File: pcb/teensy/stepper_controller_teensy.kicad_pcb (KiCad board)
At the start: 2 copper layers, 69.8 x 40.6 mm, 15 parts, among them P1 HEADER_02X08_SMD, SW1 SPST_SLIDE_AS, U1 TLE7230R

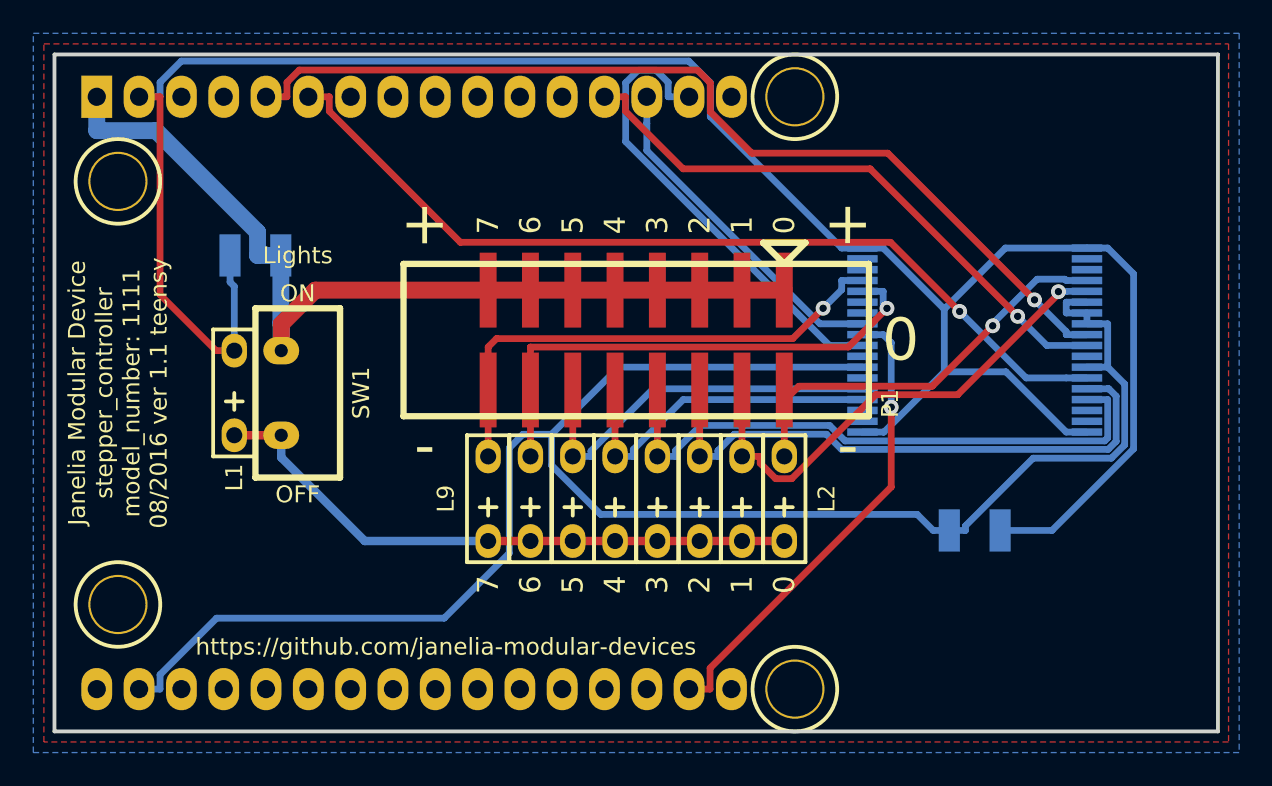
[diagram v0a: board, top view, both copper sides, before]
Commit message: Added L6470.
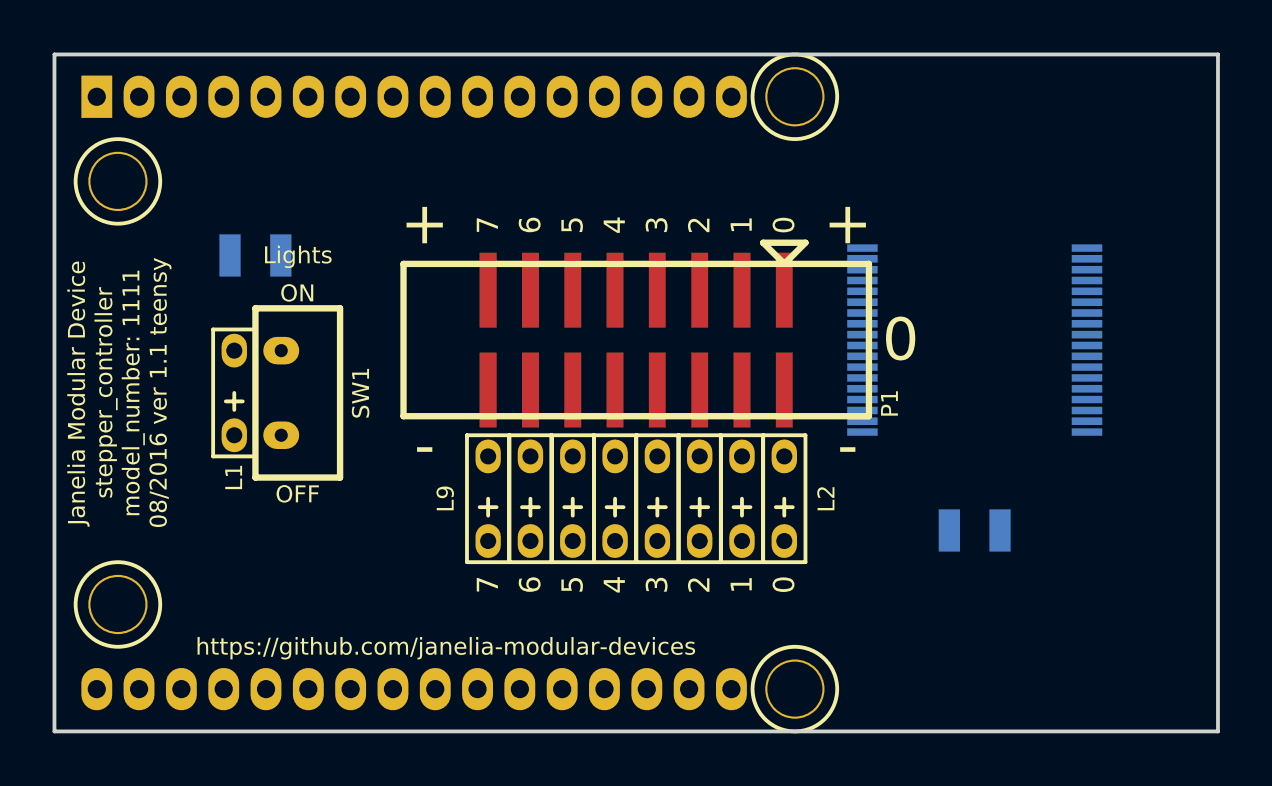
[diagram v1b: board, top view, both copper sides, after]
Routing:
- net GND: track 136.2 -> 0.00 mm
- net VEE: track 109.8 -> 0.00 mm
- net /RESET: track 58.2 -> 0.00 mm, vias 1 -> 0
- net VDD: track 55.4 -> 0.00 mm
- net /PWM: track 54.2 -> 0.00 mm, vias 1 -> 0
- net /LED_PWR: track 36.4 -> 0.00 mm
- net /OUT3: track 36.0 -> 0.00 mm
- net /CS: track 35.7 -> 0.00 mm, vias 1 -> 0
- net /OUT2: track 35.0 -> 0.00 mm
- net /OUT6: track 31.3 -> 0.00 mm, vias 1 -> 0
- net /OUT7: track 31.0 -> 0.00 mm, vias 1 -> 0
- net /OUT1: track 30.2 -> 0.00 mm, vias 1 -> 0
- net /SCK: track 28.5 -> 0.00 mm, vias 1 -> 0
- net /MISO: track 28.1 -> 0.00 mm
- net /OUT0: track 25.3 -> 0.00 mm, vias 1 -> 0
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- removed copper zone on B.Cu, net GND
- removed copper zone on F.Cu, net VDD

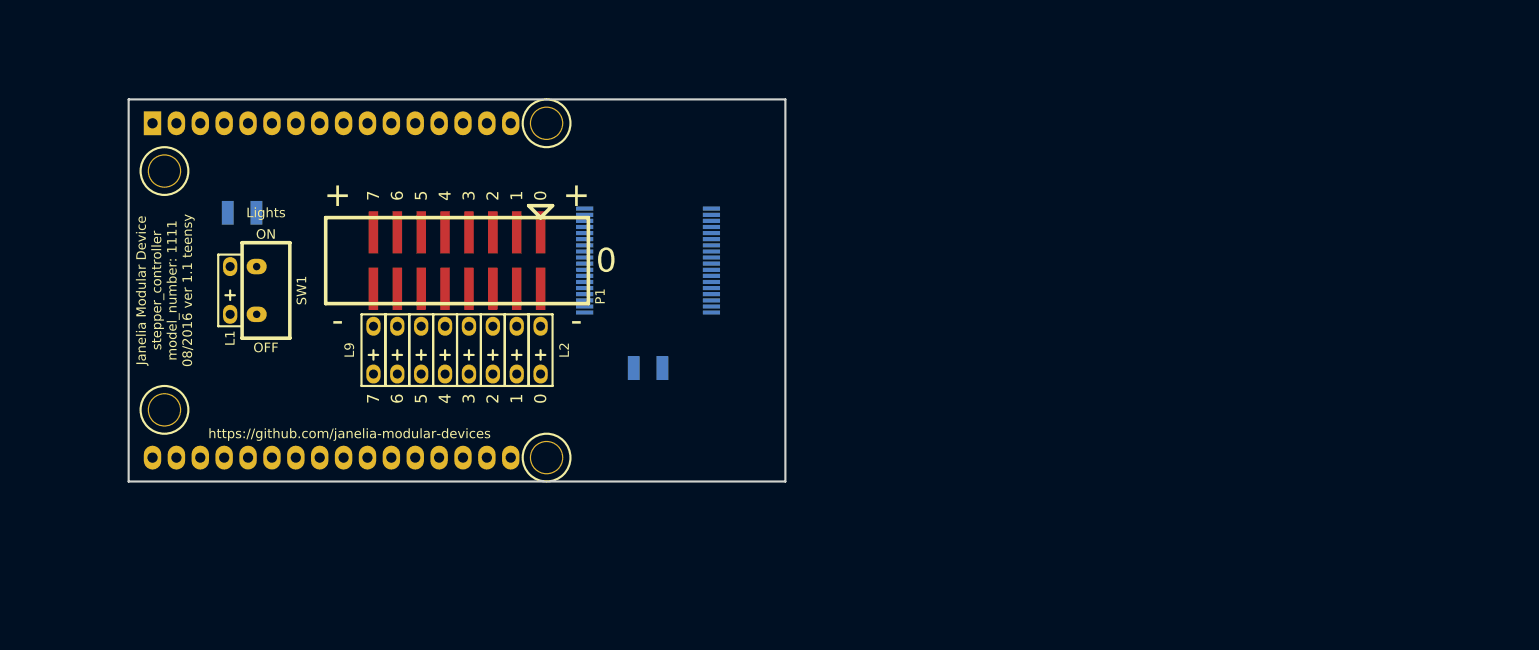
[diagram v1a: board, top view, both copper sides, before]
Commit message: Adjusted footprints.
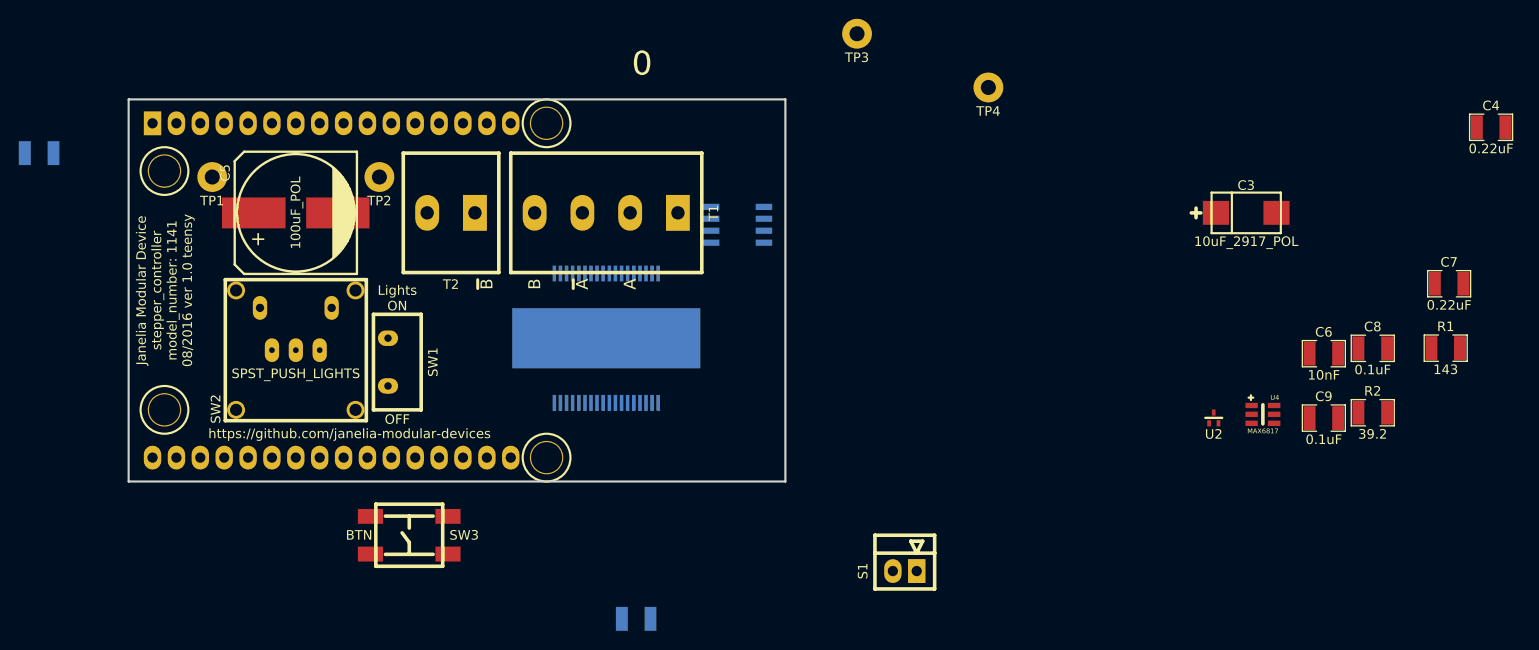
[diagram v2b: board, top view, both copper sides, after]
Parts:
- removed L1, L2, L3, L4, L5, L6, L7, L8, L9: LED_24V, stepper_controller_teensy:LED_555-3XXX
- removed P1: HEADER_02X08_SMD, stepper_controller_teensy:HEADER_02x08_SMD
- added C3: 10uF_2917_POL, stepper_controller_teensy:SM2917_POL, F.Cu at (192.5, 91.4)
- added C4: 0.22uF, stepper_controller_teensy:SM1210, F.Cu at (218.6, 82.3)
- added C5: 100uF_POL, stepper_controller_teensy:C_ELEC_12.5, F.Cu at (91.4, 91.4)
- added C6: 10nF, stepper_controller_teensy:SM1210, F.Cu at (200.8, 106.4)
- added C7: 0.22uF, stepper_controller_teensy:SM1210, F.Cu at (214.1, 99.0)
- added C8: 0.1uF, stepper_controller_teensy:SM1210, F.Cu at (206.0, 105.9)
- added C9: 0.1uF, stepper_controller_teensy:SM1210, F.Cu at (200.8, 113.3)
- added R1: 143, stepper_controller_teensy:SM1210, F.Cu at (213.7, 105.8)
- added R2: 39.2, stepper_controller_teensy:SM1210, F.Cu at (206.0, 112.7)
- added S1: HEADER_01X02_SHR, stepper_controller_teensy:Header_Shrouded_2_Pin, F.Cu at (156.2, 129.5)
- added SW2: SPST_PUSH_LIGHTS, stepper_controller_teensy:KP_SWITCH, F.Cu at (91.4, 106.0)
- added SW3: KT_SWITCH, stepper_controller_teensy:KT_SWITCH, F.Cu at (103.5, 125.7)
- added T1: TERM_BLK_ANG_4_PIN_0.2_PITCH, footprints:TERM_BLK_ANG_4_PIN_0.2_PITCH, F.Cu at (124.5, 91.4)
- added T2: TERM_BLK_ANG_2_PIN_0.2_PITCH, footprints:TERM_BLK_ANG_2_PIN_0.2_PITCH, F.Cu at (108.0, 91.4)
- added TP1: TESTPOINT_RED, footprints:TESTPOINT_THRU, F.Cu at (82.5, 87.6)
- added TP2: TESTPOINT_BLK, footprints:TESTPOINT_THRU, F.Cu at (100.3, 87.6)
- added TP3: TESTPOINT_WHT, footprints:TESTPOINT_THRU, F.Cu at (151.1, 72.4)
- added TP4: TESTPOINT_BLK, footprints:TESTPOINT_THRU, F.Cu at (165.1, 78.1)
- added U2: BAV99T, stepper_controller_teensy:SOT-523, F.Cu at (189.1, 113.2)
- added U3: CUR_SEN_+/-5A, footprints:SOIC_8_LC, B.Cu at (138.4, 92.7)
- added U4: MAX6817, stepper_controller_teensy:MAX6817, F.Cu at (194.3, 112.9)
- C1: value 10uF -> 0.1uF
- U1: value TLE7230R -> L6470; footprint stepper_controller_teensy:PG-DSO-36 -> stepper_controller_teensy:POWERSO-36
- moved C2 26.7 mm to (127.6, 134.6)
- moved C1 22.5 mm to (64.1, 85.1)
- moved SW1 15.9 mm to (102.2, 107.3)
- moved U1 9.38 mm to (124.5, 104.8), turned to 0 degrees
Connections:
- C1 pad 1: VDD -> +3V3
- C2 pad 1: VEE -> +3V3
- MDT1 pad 14: (no net) -> /VIOUT
- MDT1 pad 16: (no net) -> /LED_RED
- MDT1 pad 17: (no net) -> /LED_GREEN
- MDT1 pad 3: /PWM -> /FLAG
- MDT1 pad 3V3: (no net) -> +3V3
- MDT1 pad 4: (no net) -> /BUSY
- MDT1 pad 5: (no net) -> /ACTION
- MDT1 pad VEE: VEE -> (no net)
- SW1 pad 1: VDD -> +3V3
- U1 pad 10: /CS -> (no net)
- U1 pad 12: VEE -> GND
- U1 pad 13: /PWM -> /CP
- U1 pad 14: /OUT2 -> /VBOOT
- U1 pad 15: /OUT3 -> VDD
- U1 pad 16: (no net) -> VDD
- U1 pad 17: (no net) -> /OUT1B
- U1 pad 18: GND -> /OUT1B
- U1 pad 2: (no net) -> /OUT1A_0
- U1 pad 20: (no net) -> /OUT2B
- U1 pad 21: (no net) -> /OUT2B
- U1 pad 22: /OUT4 -> VDD
- U1 pad 23: /OUT5 -> VDD
- U1 pad 24: (no net) -> +3V3
- U1 pad 25: VEE -> /MISO
- U1 pad 26: (no net) -> /SCK
- U1 pad 27: /MISO -> /MOSI
- U1 pad 28: /SCK -> GND
- U1 pad 29: /MOSI -> /BUSY
- U1 pad 3: (no net) -> /OUT1A_0
- U1 pad 30: (no net) -> /CS
- U1 pad 31: (no net) -> /FLAG
- U1 pad 32: /OUT6 -> GND
- U1 pad 33: /OUT7 -> VDD
- U1 pad 34: (no net) -> VDD
- U1 pad 35: (no net) -> /OUT2A
- U1 pad 36: GND -> /OUT2A
- U1 pad 4: /OUT0 -> VDD
- U1 pad 5: /OUT1 -> VDD
- U1 pad 6: VEE -> /RESET
- U1 pad 7: VEE -> /SW
- U1 pad 8: VEE -> GND
- U1 pad 9: /RESET -> +3V3
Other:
- board text added: "A"
- board text added: "B"
- board text added: "Janelia Modular Device stepper_controller model_number: 1141 08/2016 ver 1.0 teensy"
- board text added: "~A"
- board text added: "~B"
- board text removed: "+"
- board text removed: "-"
- board text removed: "1"
- board text removed: "2"
- board text removed: "3"
- board text removed: "4"
- board text removed: "5"
- board text removed: "6"
- board text removed: "7"
- board text removed: "Janelia Modular Device stepper_controller model_number: 1111 08/2016 ver 1.1 teensy"

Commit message: Finished teensy pcb v1.0.
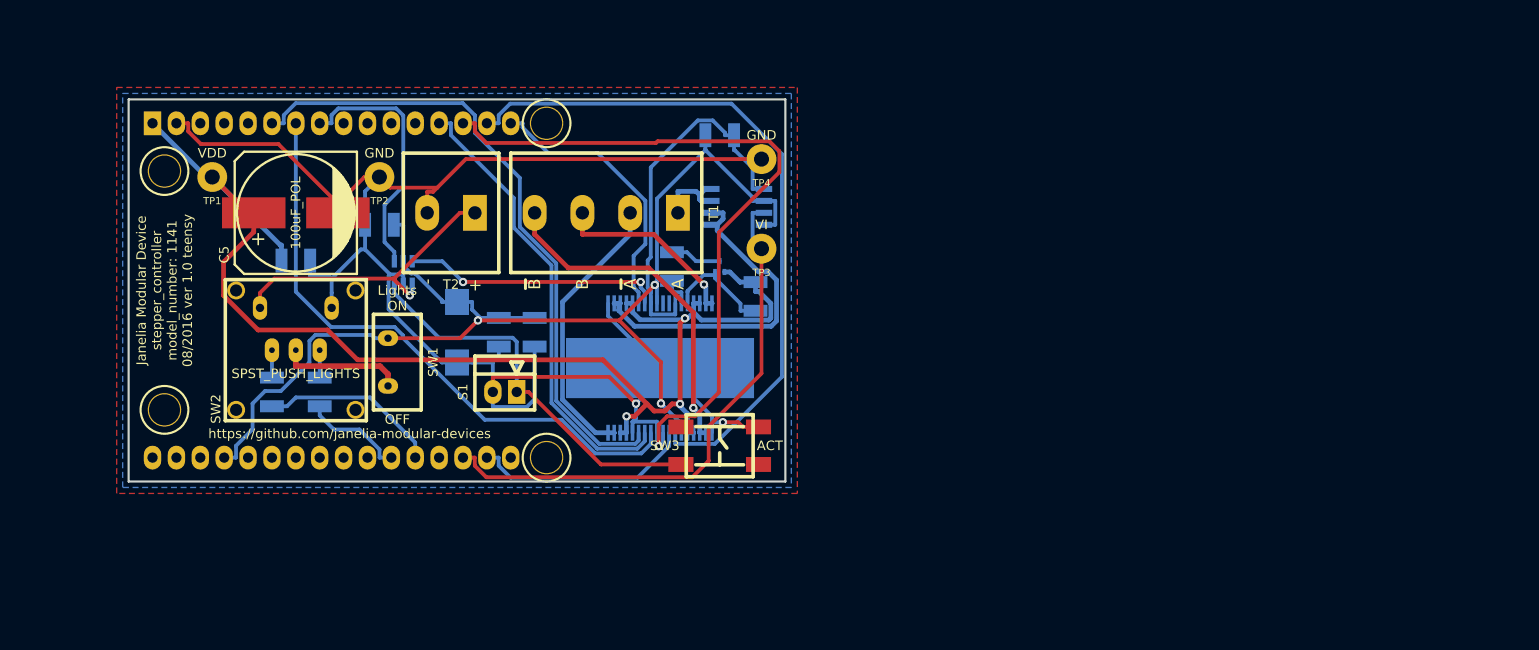
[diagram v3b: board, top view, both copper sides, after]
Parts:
- C3, C4, C6, C7, C8, C9, R1, R2, U2, U4: moved to B.Cu
- T1: footprint footprints:TERM_BLK_ANG_4_PIN_0.2_PITCH -> stepper_controller_teensy:TERM_BLK_ANG_4_PIN_0.2_PITCH
- T2: footprint footprints:TERM_BLK_ANG_2_PIN_0.2_PITCH -> stepper_controller_teensy:TERM_BLK_ANG_2_PIN_0.2_PITCH
- TP1, TP2, TP3, TP4: footprint footprints:TESTPOINT_THRU -> stepper_controller_teensy:TESTPOINT_THRU
- U3: footprint footprints:SOIC_8_LC -> stepper_controller_teensy:SOIC_8_LC
- moved C4 127.9 mm to (91.4, 96.5), turned to 180 degrees
- moved R1 124.9 mm to (88.9, 110.5), turned to 270 degrees
- moved R2 112.0 mm to (94.0, 110.5), turned to 270 degrees
- moved C9 102.5 mm to (100.3, 92.7), turned to 180 degrees
- moved U4 92.7 mm to (102.9, 97.8), turned to 90 degrees
- moved C3 84.9 mm to (108.6, 104.1), turned to 270 degrees
- moved C7 73.8 mm to (140.3, 100.3), turned to 270 degrees
- moved C8 73.1 mm to (136.5, 83.2)
- moved C6 70.0 mm to (131.4, 97.2), turned to 90 degrees
- moved C1 56.0 mm to (116.8, 104.1), turned to 270 degrees
- moved U2 55.0 mm to (136.5, 97.2), turned to 180 degrees
- moved S1 46.6 mm to (113.7, 110.5)
- moved SW3 34.4 mm to (136.5, 116.2), turned to 180 degrees
- moved C2 33.8 mm to (113.0, 104.1), turned to 270 degrees
- moved TP4 25.3 mm to (141.0, 85.7)
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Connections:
- MDT1 pad 15: (no net) -> Net-(MDT1-Pad15)
- MDT1 pad 18: (no net) -> Net-(MDT1-Pad18)
- MDT1 pad 19: (no net) -> Net-(MDT1-Pad19)
- MDT1 pad 2: /RESET -> Net-(MDT1-Pad2)
- MDT1 pad 20: (no net) -> Net-(MDT1-Pad20)
- MDT1 pad 21: (no net) -> Net-(MDT1-Pad21)
- MDT1 pad 22: (no net) -> Net-(MDT1-Pad22)
- MDT1 pad 23: (no net) -> Net-(MDT1-Pad23)
- MDT1 pad 24: (no net) -> Net-(MDT1-Pad24)
- MDT1 pad 25: (no net) -> Net-(MDT1-Pad25)
- MDT1 pad 28: (no net) -> /RESET
- MDT1 pad 29: (no net) -> Net-(MDT1-Pad29)
- MDT1 pad 30: (no net) -> Net-(MDT1-Pad30)
- MDT1 pad 6: (no net) -> Net-(MDT1-Pad6)
- MDT1 pad 9: (no net) -> Net-(MDT1-Pad9)
- MDT1 pad AGND: (no net) -> Net-(MDT1-PadAGND)
- MDT1 pad AREF: (no net) -> Net-(MDT1-PadAREF)
- MDT1 pad DAC: (no net) -> Net-(MDT1-PadDAC)
- MDT1 pad VEE: (no net) -> Net-(MDT1-PadVEE)
- U1 pad 10: (no net) -> Net-(U1-Pad10)
- U1 pad 11: (no net) -> Net-(U1-Pad11)
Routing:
- net GND: track 0.00 -> 228.1 mm, vias 0 -> 2
- net VDD: track 0.00 -> 136.8 mm, vias 0 -> 3
- net +3V3: track 0.00 -> 128.6 mm, vias 0 -> 3
- net /MOSI: track 0.00 -> 75.7 mm, vias 0 -> 1
- net /MISO: track 0.00 -> 74.1 mm
- net /FLAG: track 0.00 -> 69.1 mm
- net /BUSY: track 0.00 -> 64.6 mm
- net /VIOUT: track 0.00 -> 58.5 mm
- net /CS: track 0.00 -> 48.6 mm
- net /ACTION_B: track 0.00 -> 42.1 mm
- net /OUT2B: track 0.00 -> 36.3 mm, vias 0 -> 1
- net /OUT1A_0: track 0.00 -> 36.0 mm
- net /SW_B: track 0.00 -> 31.8 mm, vias 0 -> 1
- net /OUT2A: track 0.00 -> 29.8 mm
- net /RESET: track 0.00 -> 29.6 mm
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- added copper zone on B.Cu, net GND
- added copper zone on F.Cu, net VDD
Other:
- net class LEDPOWER: clearance 0.254 -> 0.1016; trace_width 0.508 -> 0.6096
- net class POWER: clearance 0.254 -> 0.1016; trace_width 0.8128 -> 0.4064
- net class SUPERPOWER: clearance 0.254 -> 0.1016; trace_width 1.016 -> 0.508
- board text added: "+"
- board text added: "-"
- board text added: "GND"
- board text added: "VDD"
- board text added: "VI"
- board text removed: "0"
